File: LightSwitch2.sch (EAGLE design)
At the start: 5 parts, among them SW1 SWITCH-SPST-ILLUMINATED, SW2 SWITCH-SPST-ILLUMINATED

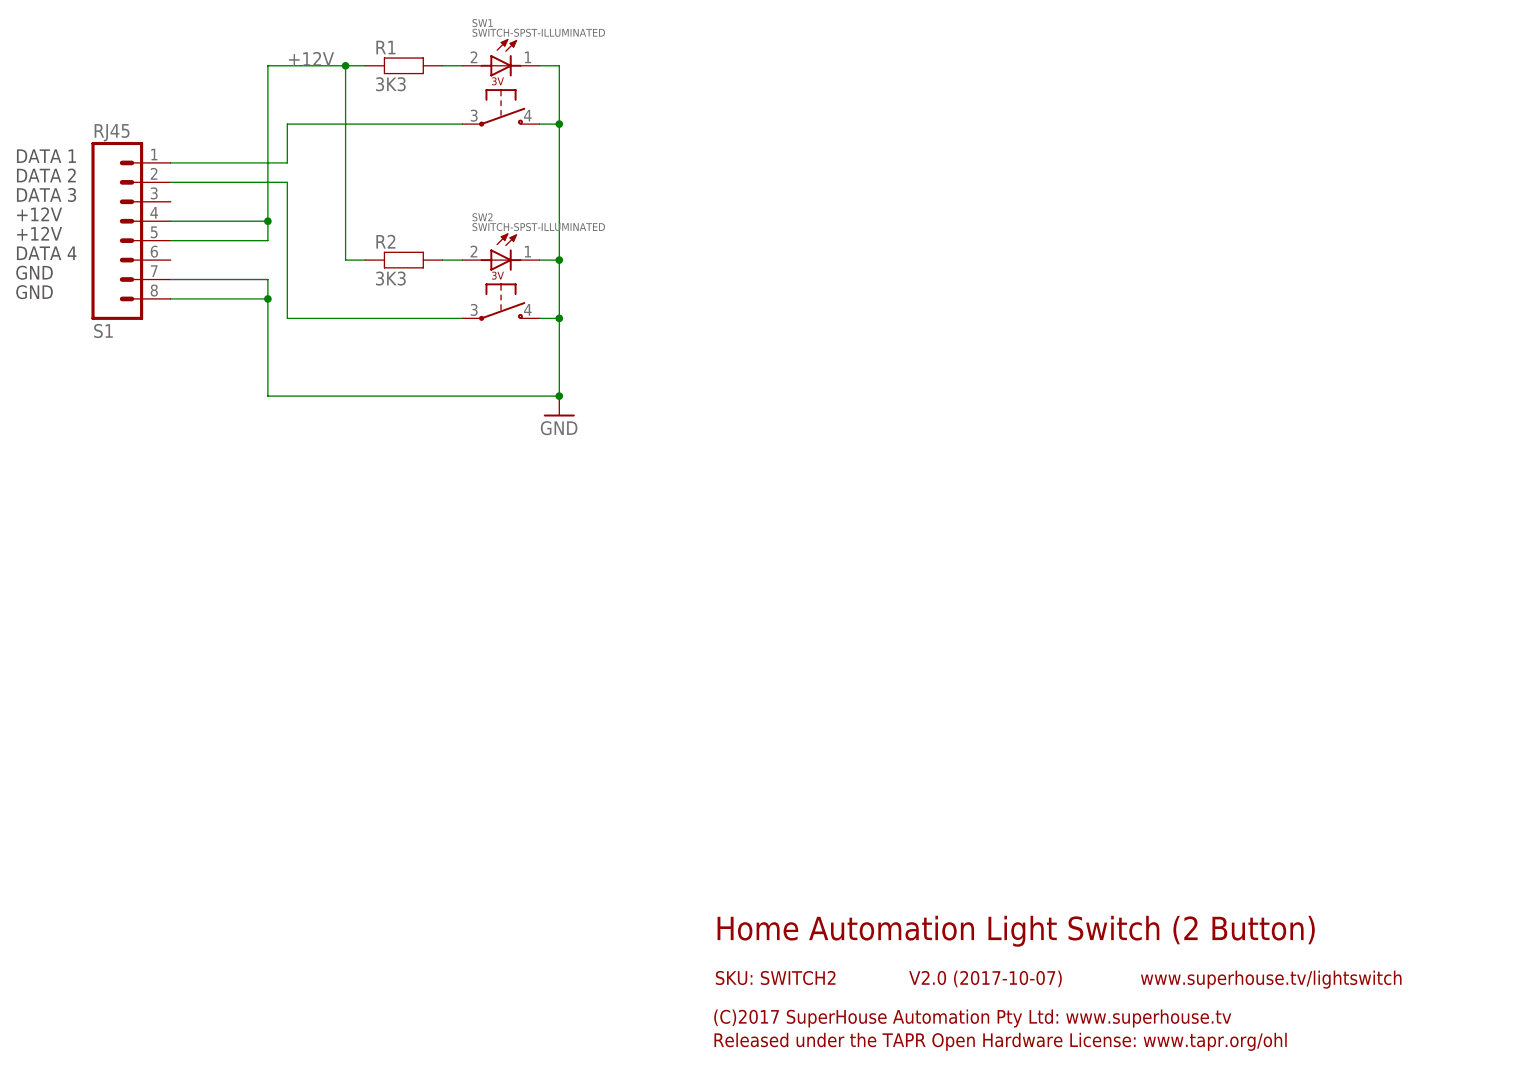
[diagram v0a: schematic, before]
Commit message: Updated button and RJ45 socket footprints for v2.2
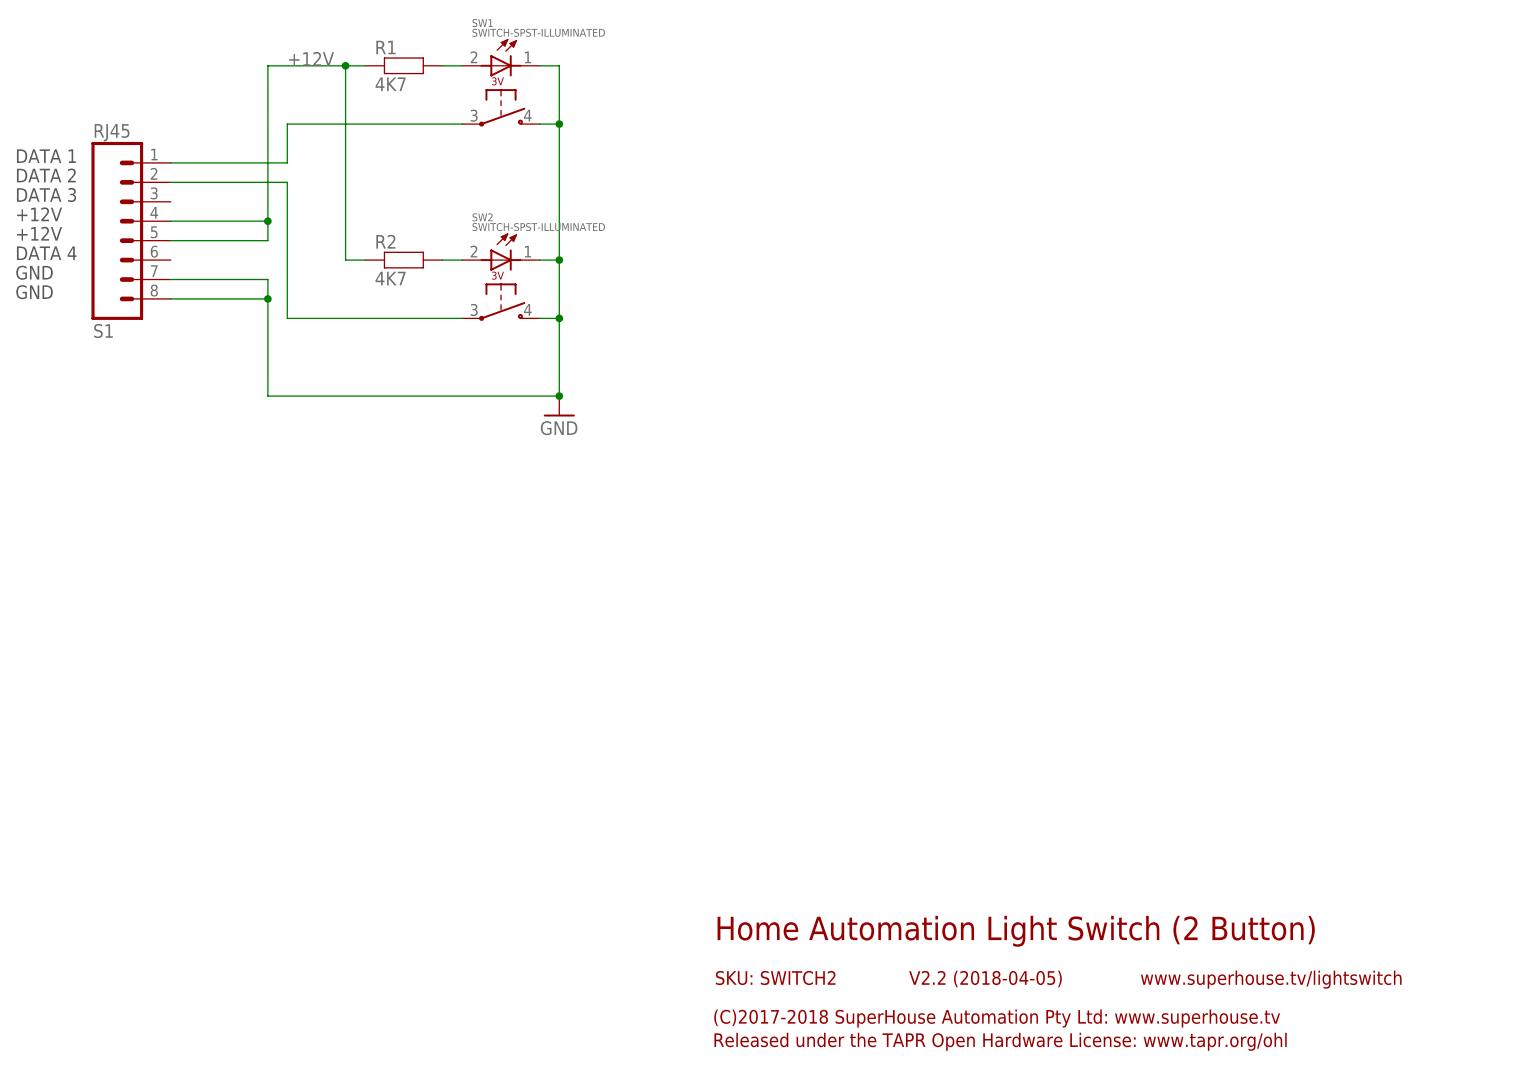
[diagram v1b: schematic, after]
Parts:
- R1, R2: value 3K3 -> 4K7
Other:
- note added: "(C)2017-2018 SuperHouse Automation Pty Ltd: www.superhouse.tv"
- note added: "V2.2 (2018-04-05)"
- note removed: "(C)2017 SuperHouse Automation Pty Ltd: www.superhouse.tv"
- note removed: "V2.0 (2017-10-07)"
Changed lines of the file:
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@@
 <?xml version="1.0" encoding="utf-8"?>
 <!DOCTYPE eagle SYSTEM "eagle.dtd">
-<eagle version="8.3.2">
+<eagle version="8.7.0">
 <drawing>
 <settings>
-<setting alwaysvectorfont="yes"/>
+<setting alwaysvectorfont="no"/>
 <setting keepoldvectorfont="yes"/>
 <setting verticaltext="up"/>
@@
 <layer number="60" name="p_dimension" color="6" fill="0" visible="no" active="no"/>
 <layer number="61" name="pt_docu" color="7" fill="0" visible="no" active="no"/>
+<layer number="88" name="SimResults" color="9" fill="1" visible="yes" active="yes"/>
+<layer number="89" name="SimProbes" color="9" fill="1" visible="yes" active="yes"/>
 <layer number="90" name="Modules" color="7" fill="1" visible="yes" active="yes"/>
 <layer number="91" name="Nets" color="2" fill="1" visible="yes" active="yes"/>
@@
 <part name="SW1" library="freetronics-jon" deviceset="SWITCH-SPST-ILLUMINATED" device=""/>
 <part name="SW2" library="freetronics-jon" deviceset="SWITCH-SPST-ILLUMINATED" device=""/>
-<part name="R1" library="freetronics-jon" deviceset="RESISTOR" device="0603" value="3K3"/>
-<part name="R2" library="freetronics-jon" deviceset="RESISTOR" device="0603" value="3K3"/>
+<part name="R1" library="freetronics-jon" deviceset="RESISTOR" device="0603" value="4K7"/>
+<part name="R2" library="freetronics-jon" deviceset="RESISTOR" device="0603" value="4K7"/>
 </parts>
 <sheets>
@@
 <frame x1="0" y1="0" x2="248.92" y2="185.42" columns="8" rows="5" layer="94"/>
 <text x="139.7" y="20.32" size="3.048" layer="94">Home Automation Light Switch (2 Button)</text>
-<text x="165.1" y="14.478" size="1.778" layer="94">V2.0 (2017-10-07)</text>
+<text x="165.1" y="14.478" size="1.778" layer="94">V2.2 (2018-04-05)</text>
 <text x="139.7" y="14.478" size="1.778" layer="94">SKU: SWITCH2</text>
-<text x="139.446" y="9.398" size="1.778" layer="94">(C)2017 SuperHouse Automation Pty Ltd: www.superhouse.tv</text>
+<text x="139.446" y="9.398" size="1.778" layer="94">(C)2017-2018 SuperHouse Automation Pty Ltd: www.superhouse.tv</text>
 <text x="139.446" y="6.35" size="1.778" layer="94">Released under the TAPR Open Hardware License: www.tapr.org/ohl</text>
 <text x="195.326" y="14.478" size="1.778" layer="94">www.superhouse.tv/lightswitch</text>

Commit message: RJ45 footprint change for v2.3
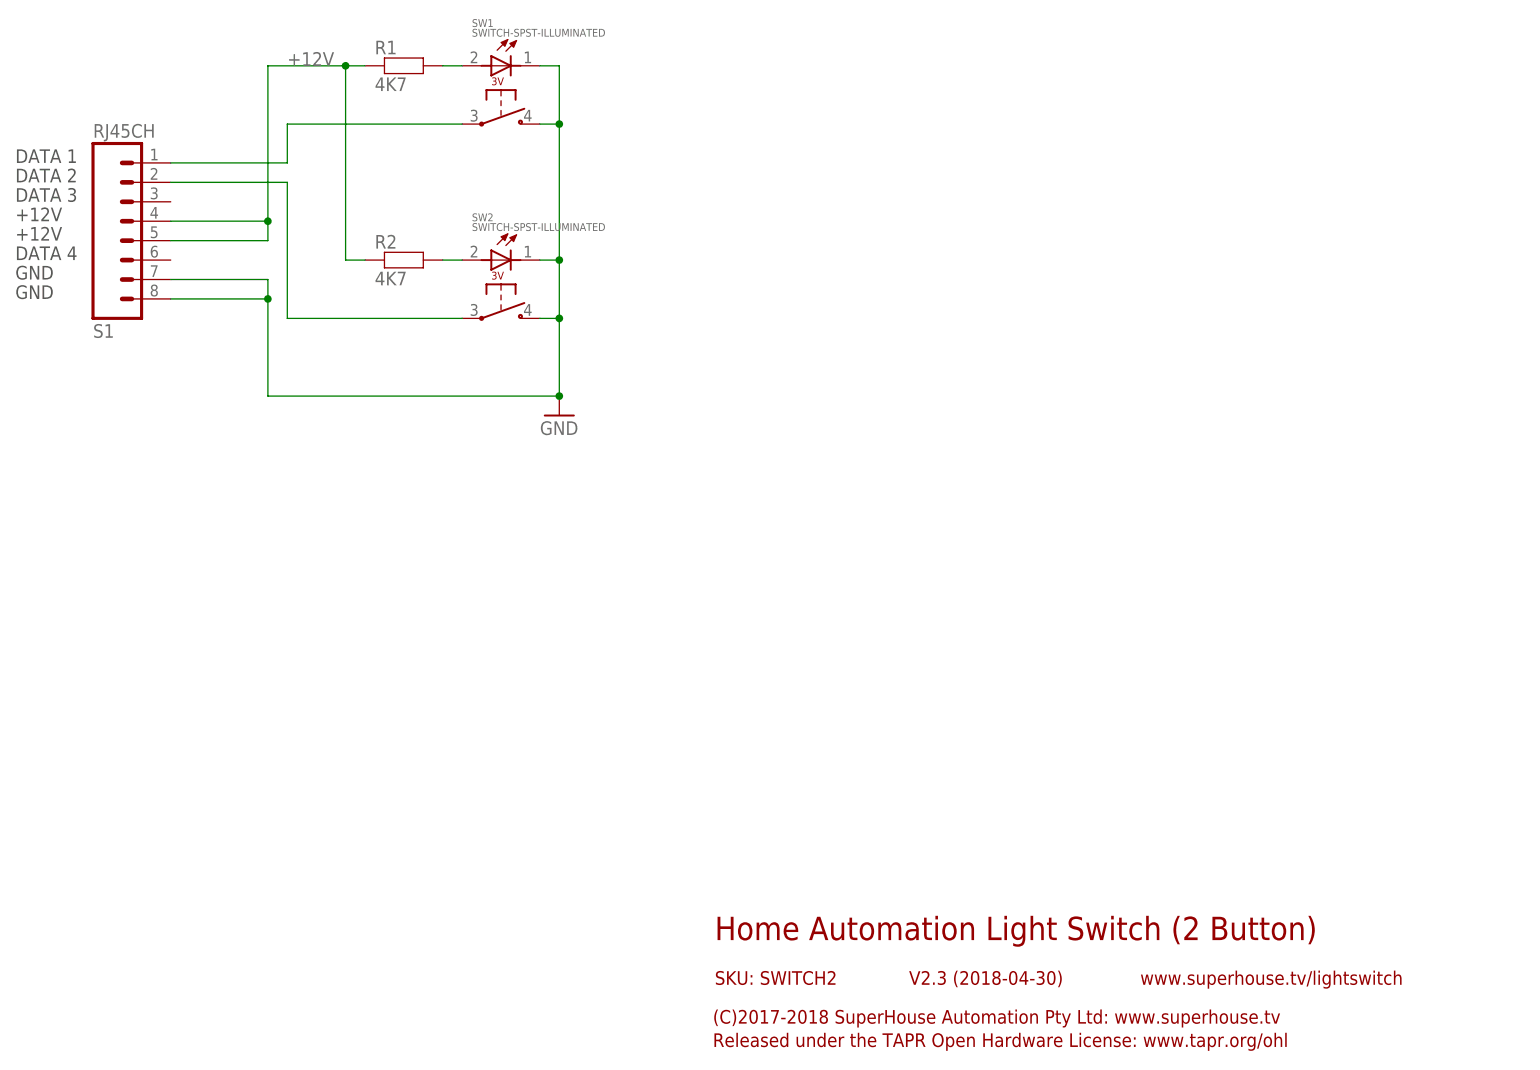
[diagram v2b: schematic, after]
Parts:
- S1: value RJ45 -> RJ45CH; device freetronics-jon:RJ45 -> freetronics-jon:RJ45CH
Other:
- note added: "V2.3 (2018-04-30)"
- note removed: "V2.2 (2018-04-05)"
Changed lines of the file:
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@@
 <?xml version="1.0" encoding="utf-8"?>
 <!DOCTYPE eagle SYSTEM "eagle.dtd">
-<eagle version="8.7.0">
+<eagle version="9.0.0">
 <drawing>
 <settings>
-<setting alwaysvectorfont="no"/>
+<setting alwaysvectorfont="yes"/>
 <setting keepoldvectorfont="yes"/>
 <setting verticaltext="up"/>
@@
 <parts>
 <part name="GND3" library="SparkFun" deviceset="GND" device=""/>
-<part name="S1" library="freetronics-jon" deviceset="RJ45" device=""/>
+<part name="S1" library="freetronics-jon" deviceset="RJ45" device="CH"/>
 <part name="SW1" library="freetronics-jon" deviceset="SWITCH-SPST-ILLUMINATED" device=""/>
 <part name="SW2" library="freetronics-jon" deviceset="SWITCH-SPST-ILLUMINATED" device=""/>
@@
 <frame x1="0" y1="0" x2="248.92" y2="185.42" columns="8" rows="5" layer="94"/>
 <text x="139.7" y="20.32" size="3.048" layer="94">Home Automation Light Switch (2 Button)</text>
-<text x="165.1" y="14.478" size="1.778" layer="94">V2.2 (2018-04-05)</text>
+<text x="165.1" y="14.478" size="1.778" layer="94">V2.3 (2018-04-30)</text>
 <text x="139.7" y="14.478" size="1.778" layer="94">SKU: SWITCH2</text>
 <text x="139.446" y="9.398" size="1.778" layer="94">(C)2017-2018 SuperHouse Automation Pty Ltd: www.superhouse.tv</text>
